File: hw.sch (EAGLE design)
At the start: 37 parts, among them IC1 MIC_I2S_SPH0645, Q3 DMG3415U, U1 MAX98357A, U2 AP2112-3.3, U3 MCP73831T-2ACI/OT, X2 JSTPH

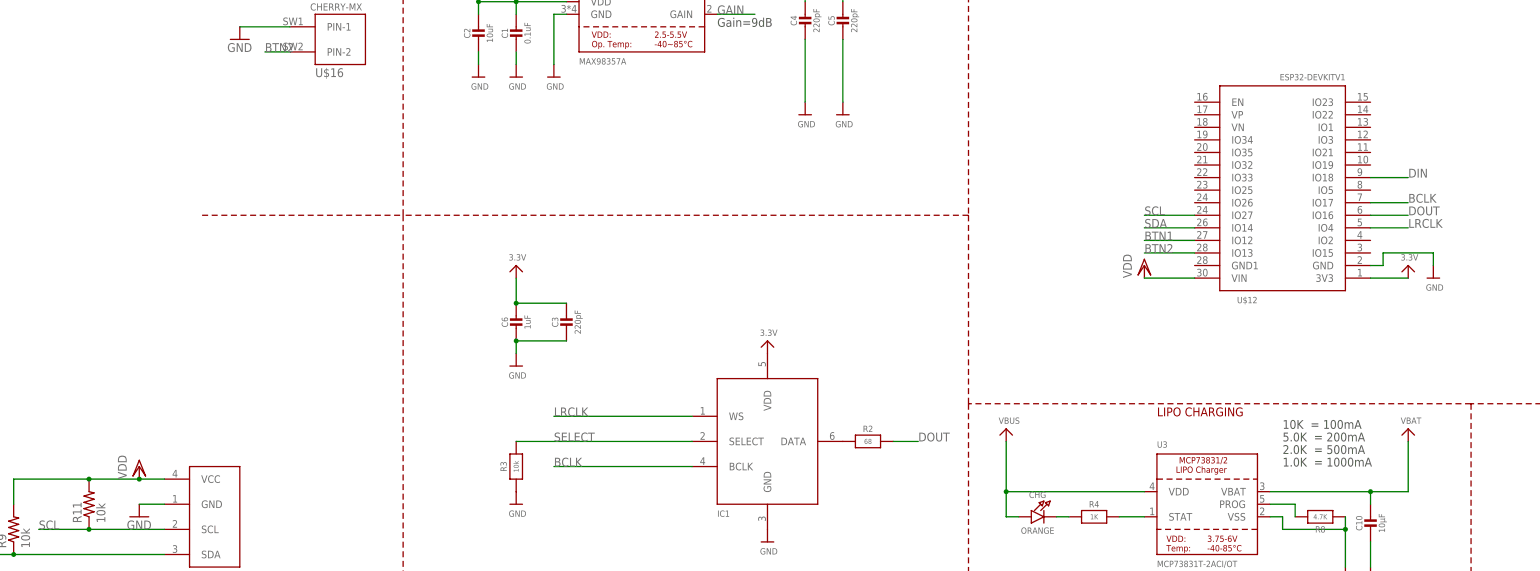
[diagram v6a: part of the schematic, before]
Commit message: flipping esp32 around
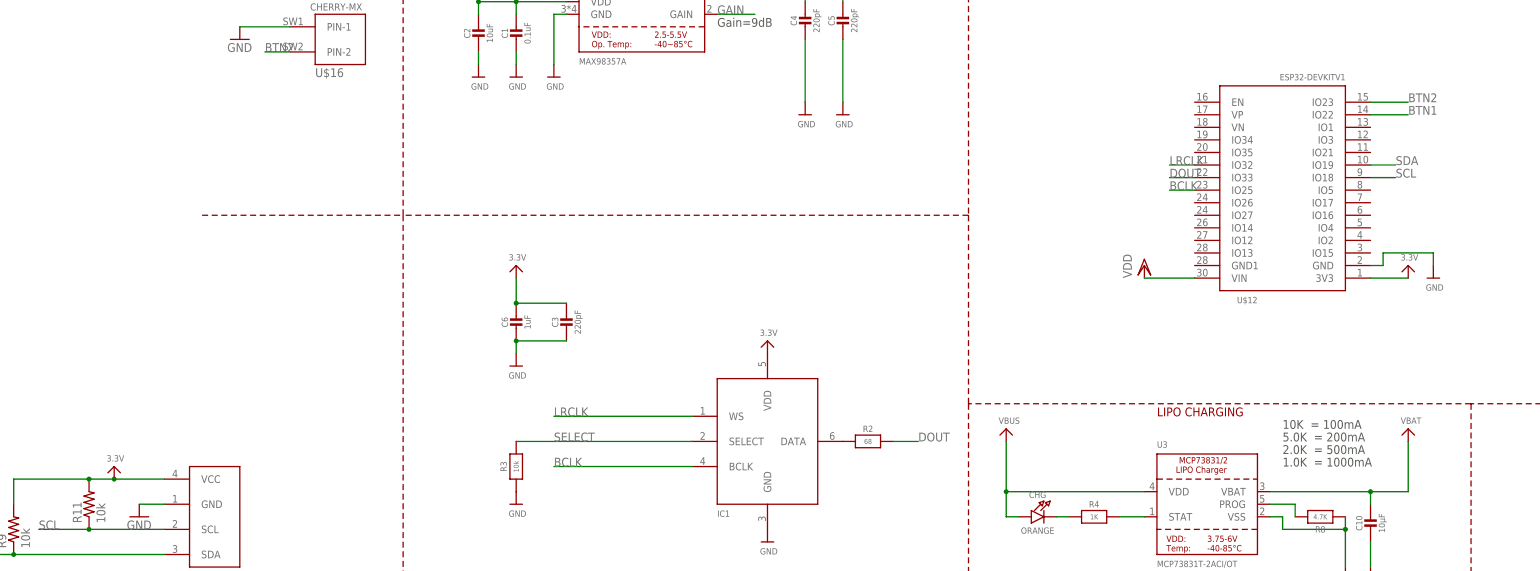
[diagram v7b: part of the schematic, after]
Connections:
- net 3.3V: now also R11.2, R9.2, U$1.VCC
- net BCLK: now also U$12.IO25; no longer U$12.IO17
- net BTN1: now also U$12.IO22; no longer U$12.IO12
- net BTN2: now also U$12.IO23; no longer U$12.IO13
- net DIN: no longer U$12.IO18
- net DOUT: now also U$12.IO33; no longer U$12.IO16
- net LRCLK: now also U$12.IO32; no longer U$12.IO4
- net SCL: now also U$12.IO18; no longer U$12.IO27
- net SDA: now also U$12.IO19; no longer U$12.IO14
- net VDD: no longer R11.2, R9.2, U$1.VCC
